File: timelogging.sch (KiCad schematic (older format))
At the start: 36 parts, among them J1 Micro_SD_Card, J2 ICSP, J3 RTC_ICSP, Q1 2N7002, Q2 16Mhz, SW1 SW_A, SW2 SW_B, U1 RP402, U2 ATMEGA328P-PU, U3 DS3231

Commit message: rework schematic
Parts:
- removed J3: RTC_ICSP, Pin_Headers:Pin_Header_Straight_2x02_Pitch2.54mm, symbol Conn_02x02_Odd_Even
- removed Q1: 2N7002, TO_SOT_Packages_SMD:SOT-23, symbol 2N7002
- removed R1, R10, R11, R2, R3, R4: 10K, Resistors_SMD:R_0805_HandSoldering, symbol R
- removed U2: ATMEGA328P-PU, Housings_QFP:TQFP-32_7x7mm_Pitch0.8mm, symbol ATMEGA328P-AU
- added C3: 10uF, Capacitors_SMD:C_0603, symbol C
- added Q1: NTR4003N, TO_SOT_Packages_SMD:SOT-23, symbol NTR4003N
- added RN1: 10K, Resistors_SMD:R_Array_Convex_4x0603, symbol R_Pack04
- added RN2: 10K, Resistors_SMD:R_Array_Convex_2x0603, symbol R_Pack02
- added U2: ATMEGA328PB-AU, Housings_QFP:TQFP-32_7x7mm_Pitch0.8mm, symbol ATMEGA328PB-AU
- C1, C2: footprint Capacitors_SMD:C_0603_HandSoldering -> Capacitors_SMD:C_0603
- C5: renamed from C4; footprint Capacitors_SMD:C_0805_HandSoldering -> Capacitors_SMD:C_0805
- C6: renamed from C5; footprint Capacitors_SMD:C_0805_HandSoldering -> Capacitors_SMD:C_0805
- C7: renamed from C6; footprint Capacitors_SMD:C_0805_HandSoldering -> Capacitors_SMD:C_0805
- D1, D2: footprint LEDs:LED_1206_HandSoldering -> LEDs:LED_1206
- L1: footprint Inductors_SMD:L_Taiyo-Yuden_NR-50xx_HandSoldering -> Inductors_SMD:L_Taiyo-Yuden_NR-50xx
- R1: renamed from R5; value 10 -> 100; footprint Resistors_SMD:R_0805_HandSoldering -> Resistors_SMD:R_0805
- R2: renamed from R6; footprint Resistors_SMD:R_0805_HandSoldering -> Resistors_SMD:R_0805
- R3: renamed from R7; footprint Resistors_SMD:R_0805_HandSoldering -> Resistors_SMD:R_0805
- R4: renamed from R8; footprint Resistors_SMD:R_0805_HandSoldering -> Resistors_SMD:R_0805
- R5: renamed from R9; footprint Resistors_SMD:R_0805_HandSoldering -> Resistors_SMD:R_0805
- R6: renamed from R12; footprint Resistors_SMD:R_0805_HandSoldering -> Resistors_SMD:R_0805
- R7: renamed from R13; footprint Resistors_SMD:R_0805_HandSoldering -> Resistors_SMD:R_0805
- R8: renamed from R14; footprint Resistors_SMD:R_0805_HandSoldering -> Resistors_SMD:R_0805
- R9: renamed from R15; footprint Resistors_SMD:R_0805_HandSoldering -> Resistors_SMD:R_0805
- U1: footprint TO_SOT_Packages_SMD:SOT-23-5_HandSoldering -> TO_SOT_Packages_SMD:SOT-23-5
- renumbered C3 to C4
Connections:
- net BTN_A: now also U2.32 ((OC3B/OC4B/INT0/PTCXY)PD2)
- net BTN_B: now also U2.1 ((OC2B/INT1/PTCXY)PD3)
- net CS: now also RN1.8 (R1.2), U2.2 ((XCK0/T0/PTCXY)PD4)
- net GND: now also C3.2, Q1.2 (S), U2.21 (GND), U2.5 (GND)
- net MISO: now also RN1.5 (R4.2), U2.16 ((MISO0/RXD1/PTCXY)PB4)
- net MOSI: now also RN1.7 (R2.2), U2.15 ((MOSI0/TXD1/OC2A/PTCXY)PB3)
- net RESET: now also U2.29 ((~RESET~)PC6)
- net SCK: now also RN1.6 (R3.2), U2.17 ((XCK0/SCK0/PTCXY)PB5)
- net SCL: now also RN2.2 (R2.1), U2.28 ((SCL0/ADC5/PTCY)PC5)
- net SDA: now also RN2.1 (R1.1), U2.27 ((SDA0/ADC4/PTCY)PC4)
- net SD_TOGGLE: now also U2.12 ((CLKO/ICP1/PTCXY)PB0)
- net VCC: now also C3.1, RN1.1 (R1.1), RN1.2 (R2.1), RN1.3 (R3.1), RN1.4 (R4.1), RN2.3 (R2.2), RN2.4 (R1.2), U2.18 (AVCC), U2.4 (VCC)
- net at D2.2 (A): now also U2.11 ((AIN1/PTCXY)PD7)
- net at D1.2 (A): now also U2.13 ((OC1A/PTCXY)PB1)
- net at C5.2, Q2.2: now also U2.7 ((XTAL1/TOSC1)PB6)
- net at C6.2, Q2.1: now also U2.8 ((XTAL2/TOSC2)PB7)
- net at J1.6 (VSS): now also Q1.3 (D)
- net at R1.1: now also Q1.1 (G)
- net at BAT_VCC1.1 (+), C1.1, L1.2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: now also U1.3 (CE)
- no-connect marks 19 -> 20
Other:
- moved on the sheet: BAT_RTC1, C2, C4, C7, D2, J1, J2, R1, R2, R4, R5, U3

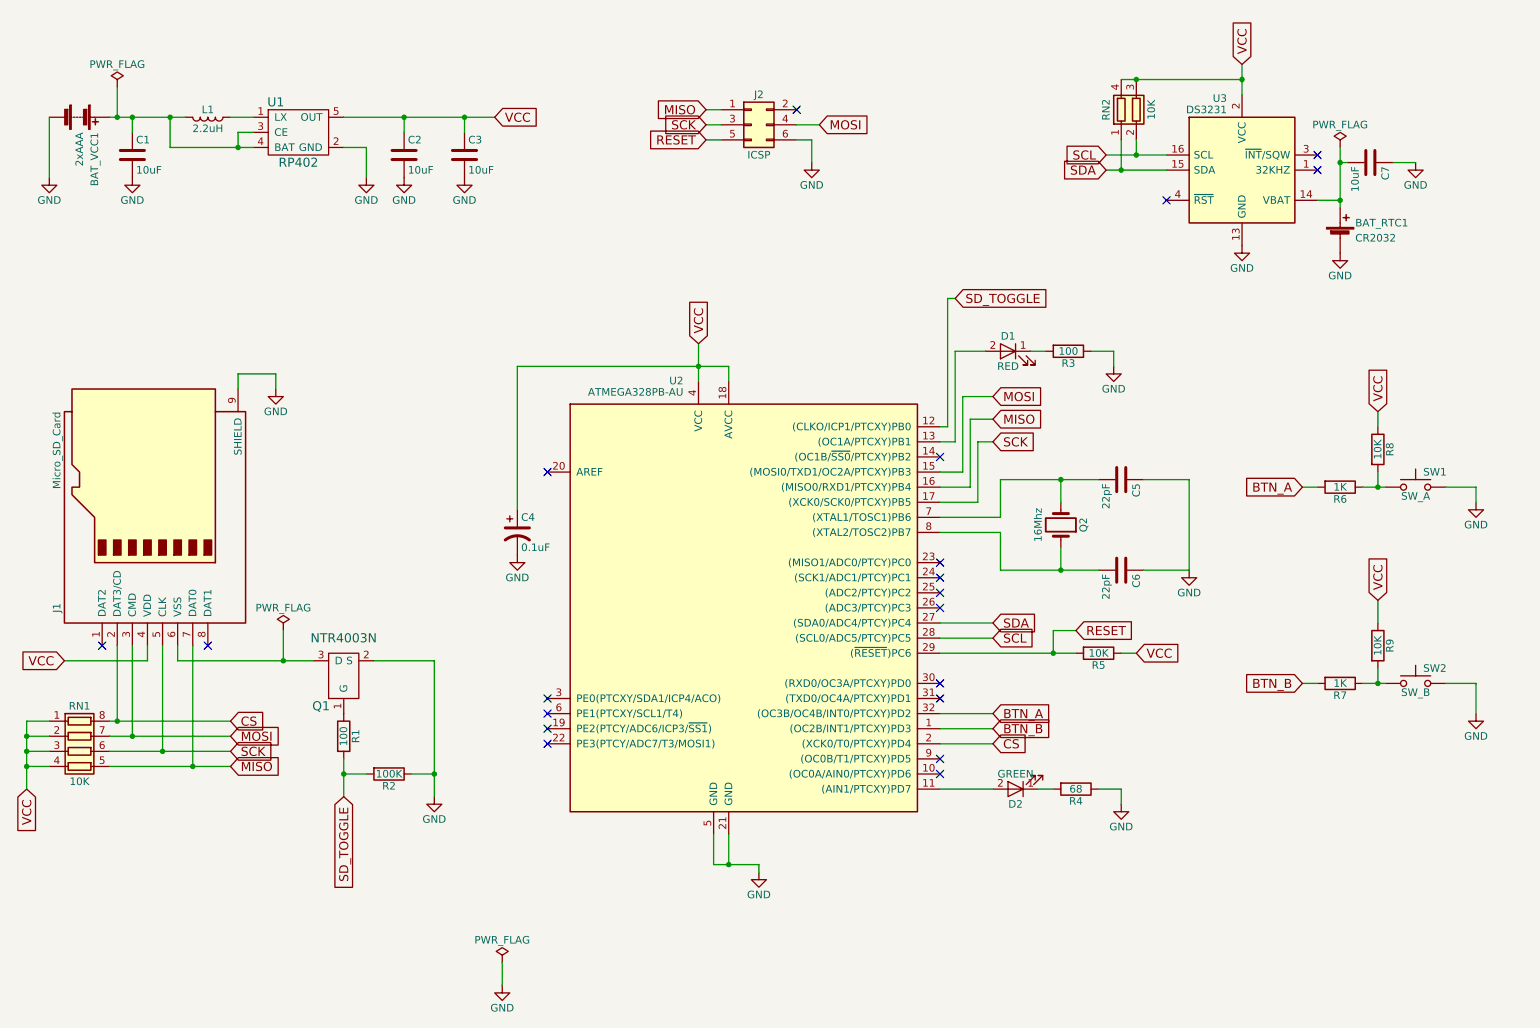
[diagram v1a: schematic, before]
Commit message: redo pcb design
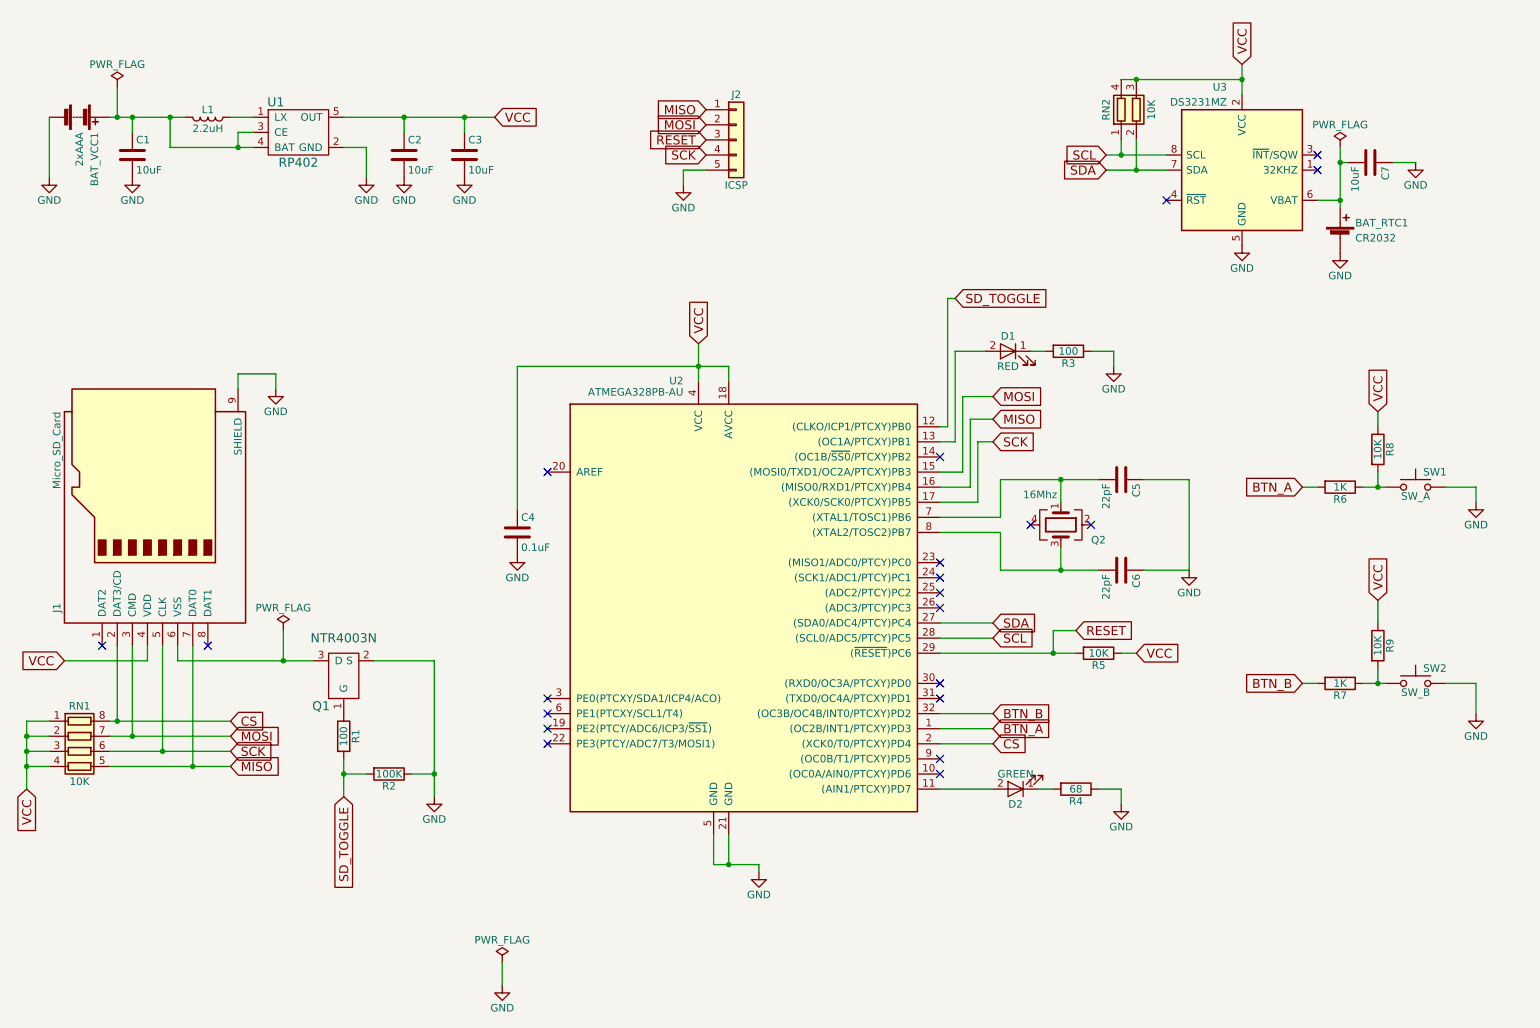
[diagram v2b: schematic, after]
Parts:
- removed C4: 0.1uF, Capacitors_Tantalum_SMD:CP_Tantalum_Case-A_EIA-3216-18_Hand, symbol CP1
- removed J2: ICSP, Pin_Headers:Pin_Header_Straight_2x03_Pitch2.54mm, symbol Conn_02x03_Odd_Even
- removed Q2: 16Mhz, Crystals:Crystal_SMD_3225-4pin_3.2x2.5mm_HandSoldering, symbol Crystal
- removed U3: DS3231, Housings_SOIC:SOIC-16W_7.5x10.3mm_Pitch1.27mm, symbol DS3231
- added C4: 0.1uF, Capacitors_SMD:C_0805, symbol C
- added J2: ICSP, Pin_Headers:Pin_Header_Straight_1x05_Pitch2.54mm_SMD_Pin1Left, symbol Conn_01x05
- added Q2: 16Mhz, Crystals:Crystal_SMD_3225-4pin_3.2x2.5mm, symbol Crystal_GND24
- added U3: DS3231MZ, Housings_SOIC:SOIC-8_3.9x4.9mm_Pitch1.27mm, symbol DS3231MZ
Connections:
- net BTN_A: now also U2.1 ((OC2B/INT1/PTCXY)PD3); no longer U2.32 ((OC3B/OC4B/INT0/PTCXY)PD2)
- net BTN_B: now also U2.32 ((OC3B/OC4B/INT0/PTCXY)PD2); no longer U2.1 ((OC2B/INT1/PTCXY)PD3)
- net GND: now also C4.2, J2.5 (Pin_5), U3.5 (GND)
- net MISO: now also J2.1 (Pin_1)
- net MOSI: now also J2.2 (Pin_2)
- net RESET: now also J2.3 (Pin_3)
- net SCK: now also J2.4 (Pin_4)
- net SCL: now also RN2.1 (R1.1), U3.8 (SCL); no longer RN2.2 (R2.1)
- net SDA: now also RN2.2 (R2.1), U3.7 (SDA); no longer RN2.1 (R1.1)
- net VCC: now also C4.1, U3.2 (VCC)
- net at BAT_RTC1.1 (+), C7.2: now also U3.6 (VBAT)
- net at C6.2, U2.8 ((XTAL2/TOSC2)PB7): now also Q2.3
- net at C5.2, U2.7 ((XTAL1/TOSC1)PB6): now also Q2.1
- no-connect marks 20 -> 21
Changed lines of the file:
@@
 LIBS:rp402
 LIBS:ntr4003n
+LIBS:ds3231
 LIBS:timelogging-cache
 EELAYER 25 0
@@
 $EndDescr
 $Comp
-L DS3231 U3
-U 1 1 5A482FAF
-P 9000 1600
-F 0 "U3" H 8900 2075 50  0000 R CNN
-F 1 "DS3231" H 8900 2000 50  0000 R CNN
-F 2 "Housings_SOIC:SOIC-16W_7.5x10.3mm_Pitch1.27mm" H 9050 1200 50  0001 L CNN
-F 3 "" H 9270 1850 50  0001 C CNN
-	1    9000 1600
-	1    0    0    -1
-$EndComp
-$Comp
 L Micro_SD_Card J1
 U 1 1 5A4830DE
@@
 $EndComp
 $Comp
-L Crystal Q2
-U 1 1 5A487B76
-P 7800 3950
-F 0 "Q2" H 7800 4100 50  0000 C CNN
-F 1 "16Mhz" H 7800 3800 50  0000 C CNN
-F 2 "Crystals:Crystal_SMD_3225-4pin_3.2x2.5mm_HandSoldering" H 7800 3950 50  0001 C CNN
-F 3 "" H 7800 3950 50  0001 C CNN
-	1    7800 3950
-	0    1    -1   0
-$EndComp
-$Comp
 L C C5
 U 1 1 5A488007
@@
 F 3 "" H 5800 6250 50  0001 C CNN
 	1    5800 6250
-	1    0    0    -1
-$EndComp
-$Comp
-L CP1 C4
-U 1 1 5A492D09
-P 4200 4000
-F 0 "C4" H 4225 4100 50  0000 L CNN
-F 1 "0.1uF" H 4225 3900 50  0000 L CNN
-F 2 "Capacitors_Tantalum_SMD:CP_Tantalum_Case-A_EIA-3216-18_Hand" H 4200 4000 50  0001 C CNN
-F 3 "" H 4200 4000 50  0001 C CNN
-	1    4200 4000
 	1    0    0    -1
 $EndComp
@@
 Wire Wire Line
 	8100 1600 8500 1600
-Connection ~ 8300 1500
-Wire Wire Line
-	8300 1400 8300 1500
-Wire Wire Line
-	8200 1600 8200 1400
-Connection ~ 8200 1600
+Wire Wire Line
+	8300 1400 8300 1600
+Wire Wire Line
+	8200 1500 8200 1400
 Wire Wire Line
 	7000 4600 7350 4600
@@
 Text GLabel 950  5700 3    60   Input ~ 0
 VCC
+Text GLabel 7350 5300 2    60   Input ~ 0
+BTN_A
 Text GLabel 7350 5200 2    60   Input ~ 0
-BTN_A
-Text GLabel 7350 5300 2    60   Input ~ 0
 BTN_B
 $Comp
@@
 NoConn ~ 7000 4400
 NoConn ~ 7000 4500
-$Comp
-L Conn_02x03_Odd_Even J2
-U 1 1 5A4DE5DB
-P 5750 1300
-F 0 "J2" H 5800 1500 50  0000 C CNN
-F 1 "ICSP" H 5800 1100 50  0000 C CNN
-F 2 "Pin_Headers:Pin_Header_Straight_2x03_Pitch2.54mm" H 5750 1300 50  0001 C CNN
-F 3 "" H 5750 1300 50  0001 C CNN
-	1    5750 1300
-	1    0    0    -1
-$EndComp
 Text GLabel 7900 4650 2    60   Input ~ 0
 RESET
@@
 L GND #PWR015
 U 1 1 5A4E6ECB
-P 6150 1550
-F 0 "#PWR015" H 6150 1300 50  0001 C CNN
-F 1 "GND" H 6150 1400 50  0000 C CNN
-F 2 "" H 6150 1550 50  0001 C CNN
-F 3 "" H 6150 1550 50  0001 C CNN
-	1    6150 1550
-	1    0    0    -1
-$EndComp
-Wire Wire Line
-	6150 1550 6150 1400
-Wire Wire Line
-	6150 1400 6050 1400
-Text GLabel 5450 1300 0    60   Input ~ 0
+P 5300 1700
+F 0 "#PWR015" H 5300 1450 50  0001 C CNN
+F 1 "GND" H 5300 1550 50  0000 C CNN
+F 2 "" H 5300 1700 50  0001 C CNN
+F 3 "" H 5300 1700 50  0001 C CNN
+	1    5300 1700
+	1    0    0    -1
+$EndComp
+Text GLabel 5450 1500 0    60   Input ~ 0
 SCK
 Text GLabel 5450 1400 0    60   Input ~ 0
 RESET
-Text GLabel 6200 1300 2    60   Input ~ 0
+Text GLabel 5450 1300 0    60   Input ~ 0
 MOSI
-Wire Wire Line
-	5550 1300 5450 1300
-Wire Wire Line
-	5450 1200 5550 1200
-Wire Wire Line
-	5450 1400 5550 1400
-Wire Wire Line
-	6050 1300 6200 1300
 $Comp
 L Battery BAT_VCC1
@@
 Wire Wire Line
 	9700 1550 9650 1550
-NoConn ~ 6050 1200
 $Comp
 L PWR_FLAG #FLG018
@@
 $EndComp
 NoConn ~ 4400 3600
+$Comp
+L DS3231MZ U3
+U 1 1 5A8DCFAE
+P 9000 1600
+F 0 "U3" H 8900 2150 50  0000 R CNN
+F 1 "DS3231MZ" H 8900 2050 50  0000 R CNN
+F 2 "Housings_SOIC:SOIC-8_3.9x4.9mm_Pitch1.27mm" H 9000 1000 50  0001 C CNN
+F 3 "" H 9000 900 50  0001 C CNN
+	1    9000 1600
+	1    0    0    -1
+$EndComp
+$Comp
+L Conn_01x05 J2
+U 1 1 5A8DE814
+P 5650 1400
+F 0 "J2" H 5650 1700 50  0000 C CNN
+F 1 "ICSP" H 5650 1100 50  0000 C CNN
+F 2 "Pin_Headers:Pin_Header_Straight_1x05_Pitch2.54mm_SMD_Pin1Left" H 5650 1400 50  0001 C CNN
+F 3 "" H 5650 1400 50  0001 C CNN
+	1    5650 1400
+	1    0    0    -1
+$EndComp
+Wire Wire Line
+	5300 1700 5300 1600
+Wire Wire Line
+	5300 1600 5450 1600
+Connection ~ 8200 1500
+Connection ~ 8300 1600
+$Comp
+L C C4
+U 1 1 5A8E0C3D
+P 4200 4000
+F 0 "C4" H 4225 4100 50  0000 L CNN
+F 1 "0.1uF" H 4225 3900 50  0000 L CNN
+F 2 "Capacitors_SMD:C_0805" H 4238 3850 50  0001 C CNN
+F 3 "" H 4200 4000 50  0001 C CNN
+	1    4200 4000
+	1    0    0    -1
+$EndComp
+$Comp
+L Crystal_GND24 Q2
+U 1 1 5A948BFD
+P 7800 3950
+F 0 "Q2" V 7900 4150 50  0000 L CNN
+F 1 "16Mhz" V 7600 3700 50  0000 L CNN
+F 2 "Crystals:Crystal_SMD_3225-4pin_3.2x2.5mm" H 7800 3950 50  0001 C CNN
+F 3 "" H 7800 3950 50  0001 C CNN
+	1    7800 3950
+	0    1    1    0
+$EndComp
+NoConn ~ 8000 3950
+NoConn ~ 7600 3950
 $EndSCHEMATC
